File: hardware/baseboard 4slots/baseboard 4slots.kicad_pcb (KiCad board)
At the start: 2 copper layers, 354 x 60 mm, 24 parts, among them J1 IO-Board_00, J2 IO-Board_01, J3 IO-Board_10, J4 IO-Board_11, J5 USB_B_Micro, J6 Conn_01x05: Adafruit 1833, J7 Screw_Terminal_01x04, J8 Conn_02x02_Odd_Even, J9 Conn_02x02_Odd_Even, U1 NRF24L01_Breakout, U2 Pico

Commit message: Baseboard: Add some capacitors between GND and supply lines (nRF24 connector, RPi Pico, status LEDs and IO connectors)
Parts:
- added C1: 100nF, Capacitor_SMD:C_0603_1608Metric, F.Cu at (170.0, 44.8)
- added C2: 100nF, Capacitor_SMD:C_0603_1608Metric, F.Cu at (231.2, 45.8)
- added C3: 100nF, Capacitor_SMD:C_0603_1608Metric, F.Cu at (217.8, 33.1)
- added C4: 100nF, Capacitor_SMD:C_0603_1608Metric, F.Cu at (60.3, 82.6)
- added C5: 100nF, Capacitor_SMD:C_0603_1608Metric, F.Cu at (166.2, 82.6)
- added C6: 100nF, Capacitor_SMD:C_0603_1608Metric, F.Cu at (272.4, 82.6)
- added C7: 100nF, Capacitor_SMD:C_0603_1608Metric, F.Cu at (344.5, 82.7)
- added C8: 100nF, Capacitor_SMD:C_0603_1608Metric, F.Cu at (220.8, 45.3)
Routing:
- net VDD: track 536.7 -> 544.2 mm
- net +3V3: track 501.7 -> 504.0 mm
- net GND: vias 80 -> 85

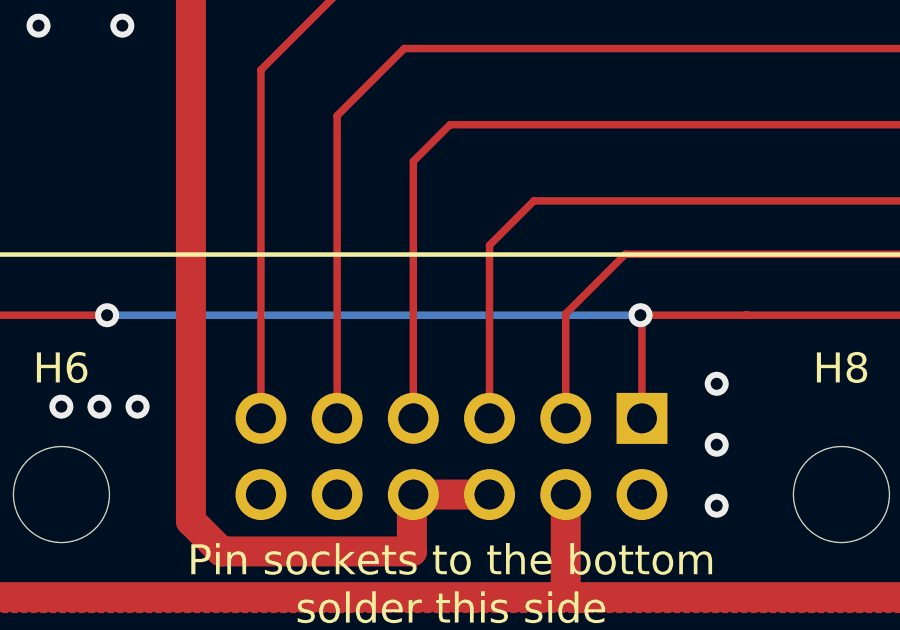
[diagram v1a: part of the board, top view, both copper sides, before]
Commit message: Fix IO connector labelling
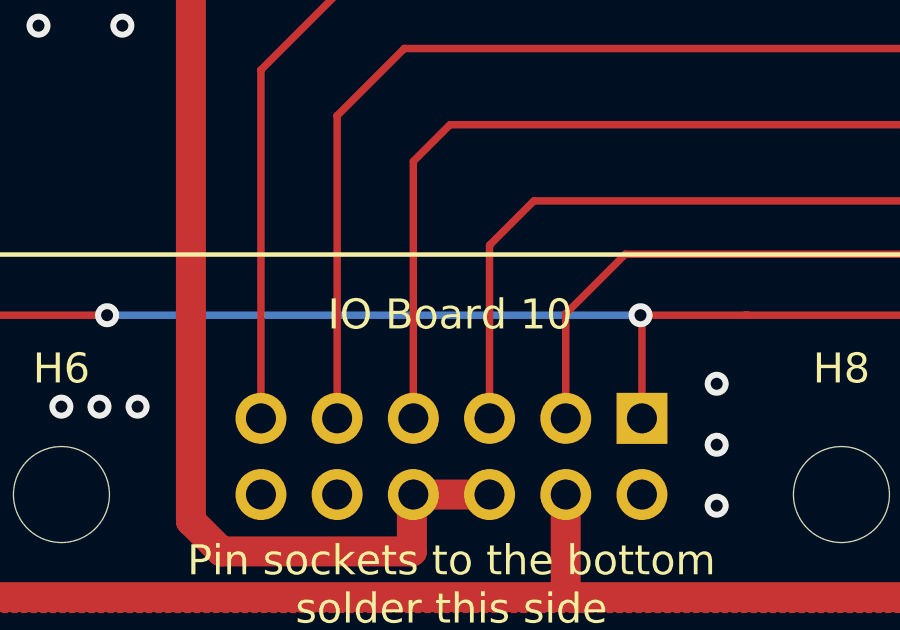
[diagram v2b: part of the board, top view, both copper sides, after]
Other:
- board text added: "IO Board 10"

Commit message: Hardware: Several fixes and improvements in schematics and PCBs (more capacitors, alternative footprint for DC/DC converter, more GND stitching, better trace placement, ...)
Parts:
- added C10: 1nF, Capacitor_SMD:C_0603_1608Metric, F.Cu at (168.8, 82.7)
- added C11: 1nF, Capacitor_SMD:C_0603_1608Metric, F.Cu at (274.8, 82.7)
- added C12: 1nF, Capacitor_SMD:C_0603_1608Metric, F.Cu at (341.7, 82.6)
- added C13: 1nF, Capacitor_SMD:C_0603_1608Metric, F.Cu at (168.4, 45.8)
- added C9: 1nF, Capacitor_SMD:C_0603_1608Metric, F.Cu at (62.2, 82.7)
- moved C1 1.00 mm to (170.0, 45.8)
- moved C7 0.76 mm to (343.8, 82.6)
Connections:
- J6 pad 1: (no net) -> GND
- J8 pad 1: (no net) -> GND
- J8 pad 2: (no net) -> GND
- J8 pad 3: (no net) -> GND
- J8 pad 4: (no net) -> GND
- J9 pad 1: (no net) -> GND
- J9 pad 2: (no net) -> GND
- J9 pad 3: (no net) -> GND
- J9 pad 4: (no net) -> GND
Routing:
- net +3V3: track 504.0 -> 529.4 mm, vias 5 -> 7
- net VDD: track 544.2 -> 553.1 mm
- net Net-(D1-Pad2): track 44.1 -> 46.8 mm
- net GND: vias 85 -> 229
- net /STATUS_LEDS: vias 2 -> 0
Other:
- board text added: "Mechanical stands GND connection pins to the bottom solder this side"
- board text removed: "Mechanical stands No electric connection pins to the bottom solder this side"

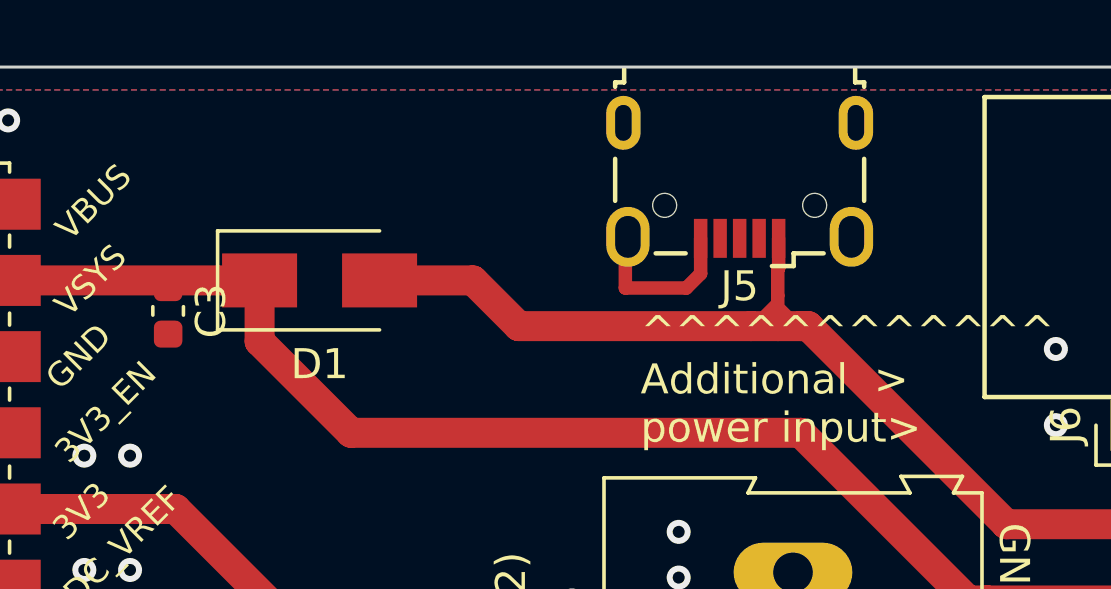
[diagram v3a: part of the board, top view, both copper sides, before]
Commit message: Silk screen and GND plane improvements
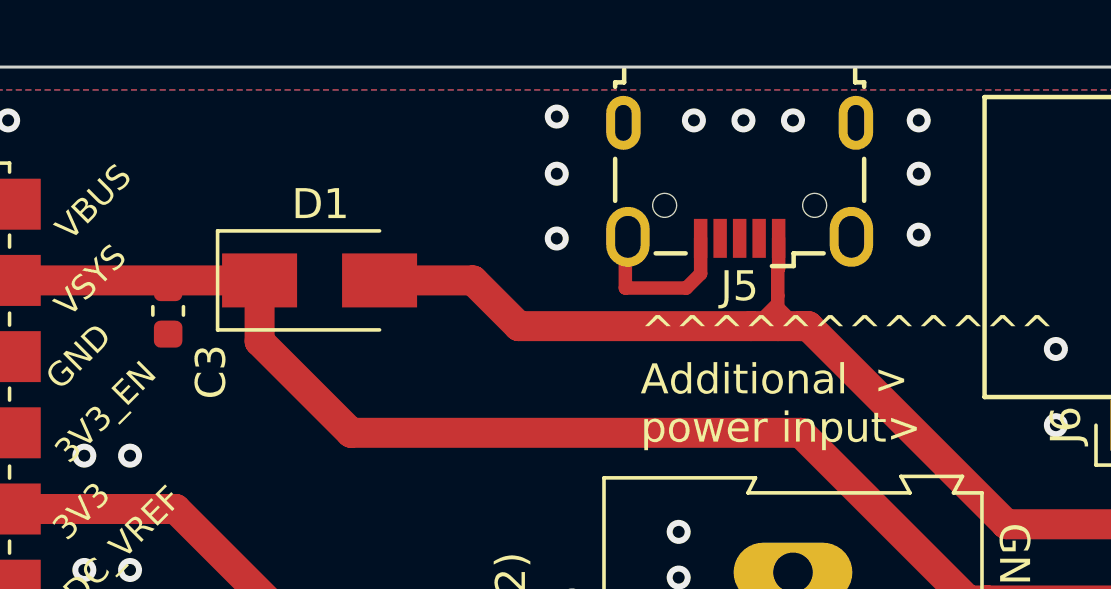
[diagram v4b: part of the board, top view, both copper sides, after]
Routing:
- net GND: vias 229 -> 238

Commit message: Add LCSC part numbers to the schematic for production :)
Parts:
- D1: value D_Schottky -> SS14
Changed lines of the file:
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@@
   (general
     (thickness 1.6)
-    (drawings 54)
+    (drawings 53)
     (tracks 597)
     (zones 0)
@@
     (visible_elements FFFFFF7F)
     (pcbplotparams
-      (layerselection 0x010fc_ffffffff)
+      (layerselection 0x010f0_ffffffff)
       (usegerberextensions false)
       (usegerberattributes true)
@@
       (outputformat 1)
       (mirror false)
-      (drillshape 1)
+      (drillshape 0)
       (scaleselection 1)
-      (outputdirectory ""))
+      (outputdirectory "plots/"))
   )
   (net 0 "")
@@
       (effects (font (size 0.5 0.5) (thickness 0.08)))
     )
-    (pad 2 smd roundrect (at 1 0) (size 1.2 1.4) (layers F.Cu F.Paste F.Mask) (roundrect_rratio 0.208333)
+    (pad 2 smd roundrect (at 1 0) (size 1.2 1.4) (layers F.Cu F.Paste F.Mask) (roundrect_rratio 0.2083325)
       (net 9 /SCL))
-    (pad 1 smd roundrect (at -1 0) (size 1.2 1.4) (layers F.Cu F.Paste F.Mask) (roundrect_rratio 0.208333)
+    (pad 1 smd roundrect (at -1 0) (size 1.2 1.4) (layers F.Cu F.Paste F.Mask) (roundrect_rratio 0.2083325)
       (net 3 +3V3))
     (model ${KISYS3DMOD}/Resistor_SMD.3dshapes/R_0805_2012Metric.wrl
@@
       (effects (font (size 0.5 0.5) (thickness 0.08)))
     )
-    (pad 2 smd roundrect (at 1 0) (size 1.2 1.4) (layers F.Cu F.Paste F.Mask) (roundrect_rratio 0.208333)
+    (pad 2 smd roundrect (at 1 0) (size 1.2 1.4) (layers F.Cu F.Paste F.Mask) (roundrect_rratio 0.2083325)
       (net 10 /SDA))
-    (pad 1 smd roundrect (at -1 0) (size 1.2 1.4) (layers F.Cu F.Paste F.Mask) (roundrect_rratio 0.208333)
+    (pad 1 smd roundrect (at -1 0) (size 1.2 1.4) (layers F.Cu F.Paste F.Mask) (roundrect_rratio 0.2083325)
       (net 3 +3V3))
     (model ${KISYS3DMOD}/Resistor_SMD.3dshapes/R_0805_2012Metric.wrl
@@
       (effects (font (size 1 1) (thickness 0.15)))
     )
-    (fp_text value D_Schottky (at 0 2.6) (layer F.Fab)
+    (fp_text value SS14 (at 0 2.6) (layer F.Fab)
       (effects (font (size 1 1) (thickness 0.15)))
     )
@@
   (gr_line (start 25 85) (end 25 25) (layer Edge.Cuts) (width 0.1))
   (gr_line (start 379 85) (end 25 85) (layer Edge.Cuts) (width 0.1))
-  (target plus (at 25 25) (size 5) (width 0.1) (layer Edge.Cuts))
   (via (at 234.804 54.972) (size 0.8) (drill 0.4) (layers F.Cu B.Cu) (net 1))
   (via (at 234.804 56.75) (size 0.8) (drill 0.4) (layers F.Cu B.Cu) (net 1))
